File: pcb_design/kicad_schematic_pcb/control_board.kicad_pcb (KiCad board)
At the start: 2 copper layers, 62.4 x 72.6 mm, 26 parts, among them IC1 PIC24FJ64GA002-I_SP, J1 PICkit3 - ICSP, J19 Conn_01x02_Pin

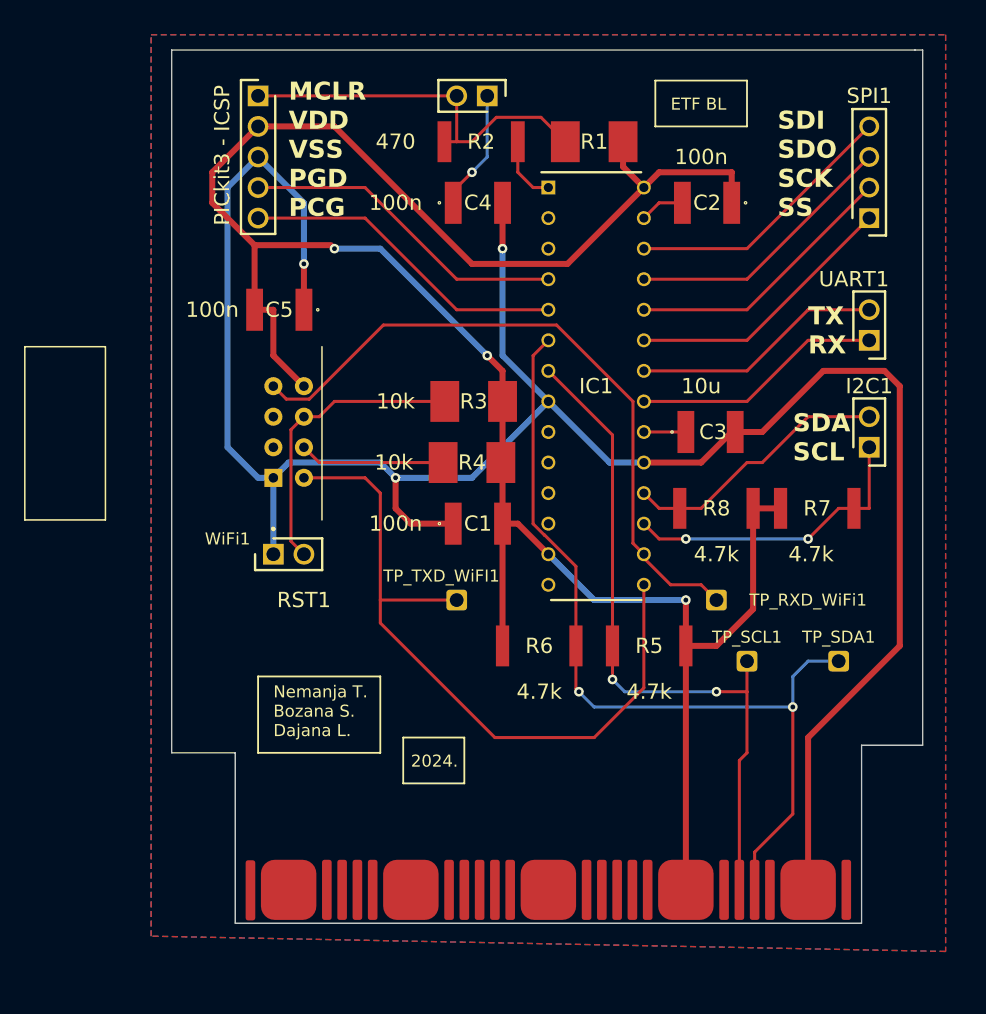
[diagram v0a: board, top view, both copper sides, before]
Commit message: Issue #22 : Rutiranje PCB-a
 - Izmjene footprint-a svih otpornika

 - Izmjene rutiranja komponenata u skladu sa primjedbama
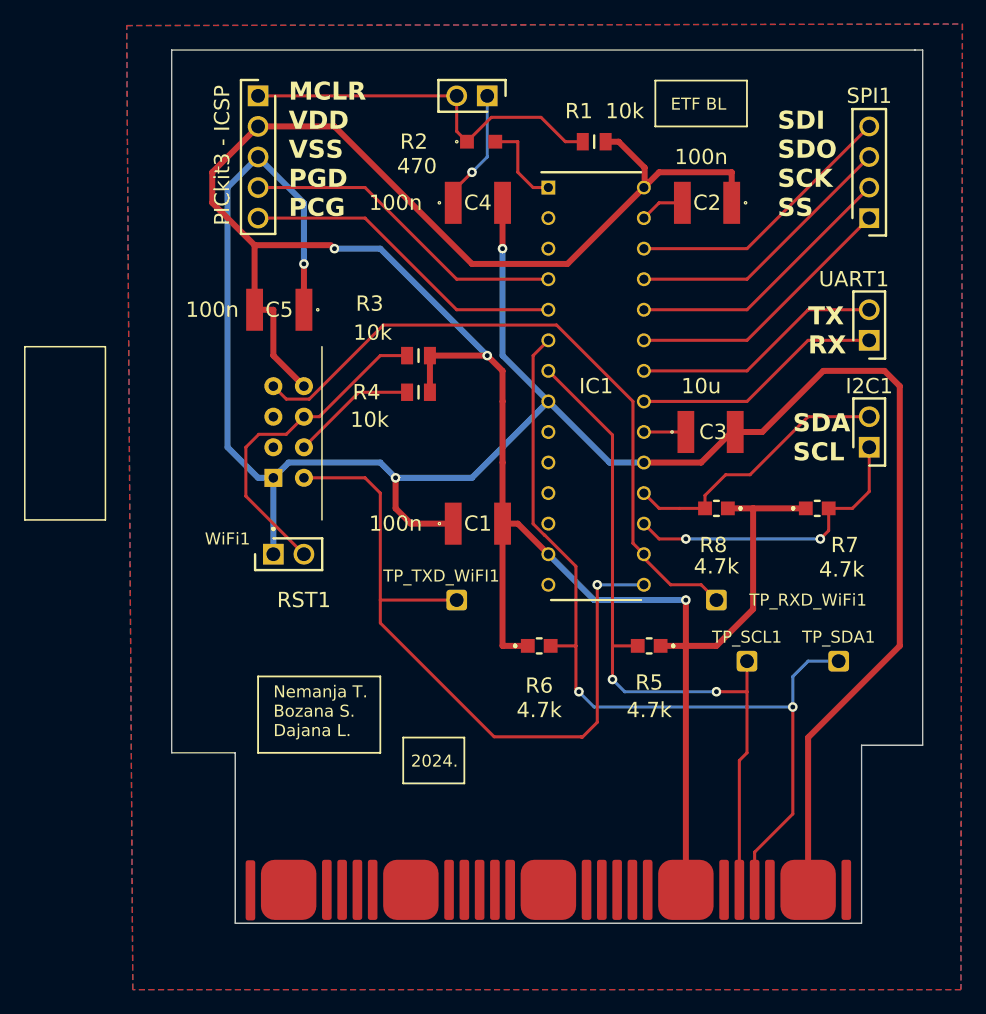
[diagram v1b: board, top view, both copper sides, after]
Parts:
- R1, R3, R4: footprint RES_10k:RESC6432X120N -> RES_10k_new:RESC2012X65N
- R2: footprint RES_470:RESC6332X65N -> RES_470_new:ERA6VK
- R5, R6, R7, R8: footprint RES_4k7:RESC6432X65N -> RES_4k7_new:ERA6AEB1020V
- moved R4 7.34 mm to (120.0, 84.3)
- moved R3 5.96 mm to (120.0, 81.3)
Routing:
- net VDD: track 187.7 -> 205.1 mm
- net Net-(RST1-Pin_2): track 24.6 -> 27.4 mm
- net Net-(IC1-AN5/C1IN+/RP3/SCL2/CN7/RB3): track 57.5 -> 59.6 mm
- net Net-(IC1-AN4/C1IN-/RP2/SDA2/CN6/RB2): track 73.0 -> 75.1 mm
- net Net-(IC1-~{MCLR}): track 5.80 -> 7.68 mm
- net Net-(IC1-PGC3/EMUC3/RP6/ASCL1/CN24/PMD6/RB6): track 60.2 -> 61.8 mm, vias 0 -> 1
- net Net-(WiFi1-EN): track 12.1 -> 10.5 mm
